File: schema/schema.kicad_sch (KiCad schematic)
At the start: 13 parts, among them Q1 2N7000, SW1 SW_Push, U1 PIC32MX170F256B, U2 NRF24L01_Breakout

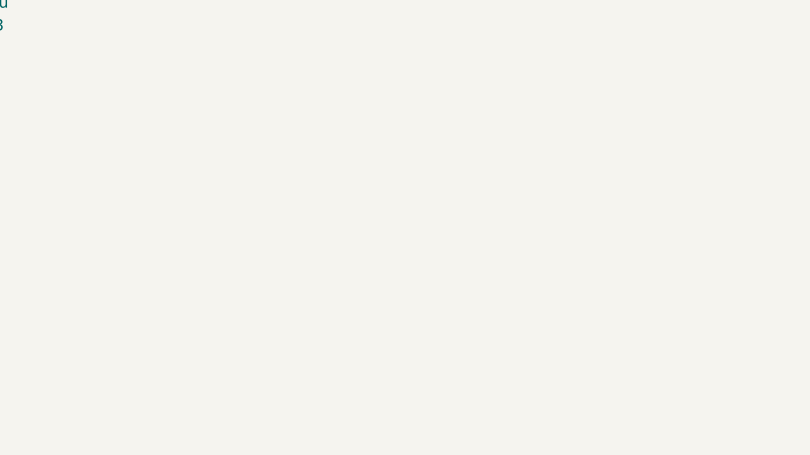
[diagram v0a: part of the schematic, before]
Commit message: Update schematic. Remote motor control working
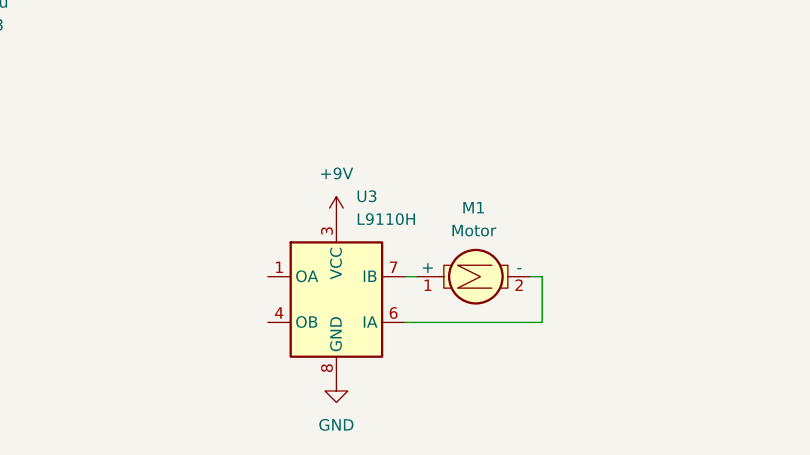
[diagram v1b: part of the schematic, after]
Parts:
- added M1: Motor, symbol ME218_BaseLib:Motor
- added U3: L9110H, Package_SO:SOIC-8_3.9x4.9mm_P1.27mm, symbol Driver_FET:HIP2100_SOIC
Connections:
- net GND: now also U3.5 (GND), U3.8 (GND)
- new net: M1.2 (-), U3.6 (IA)
- new net: M1.1 (+), U3.7 (IB)
- new net +9V: U3.2 (VCC), U3.3 (VCC)

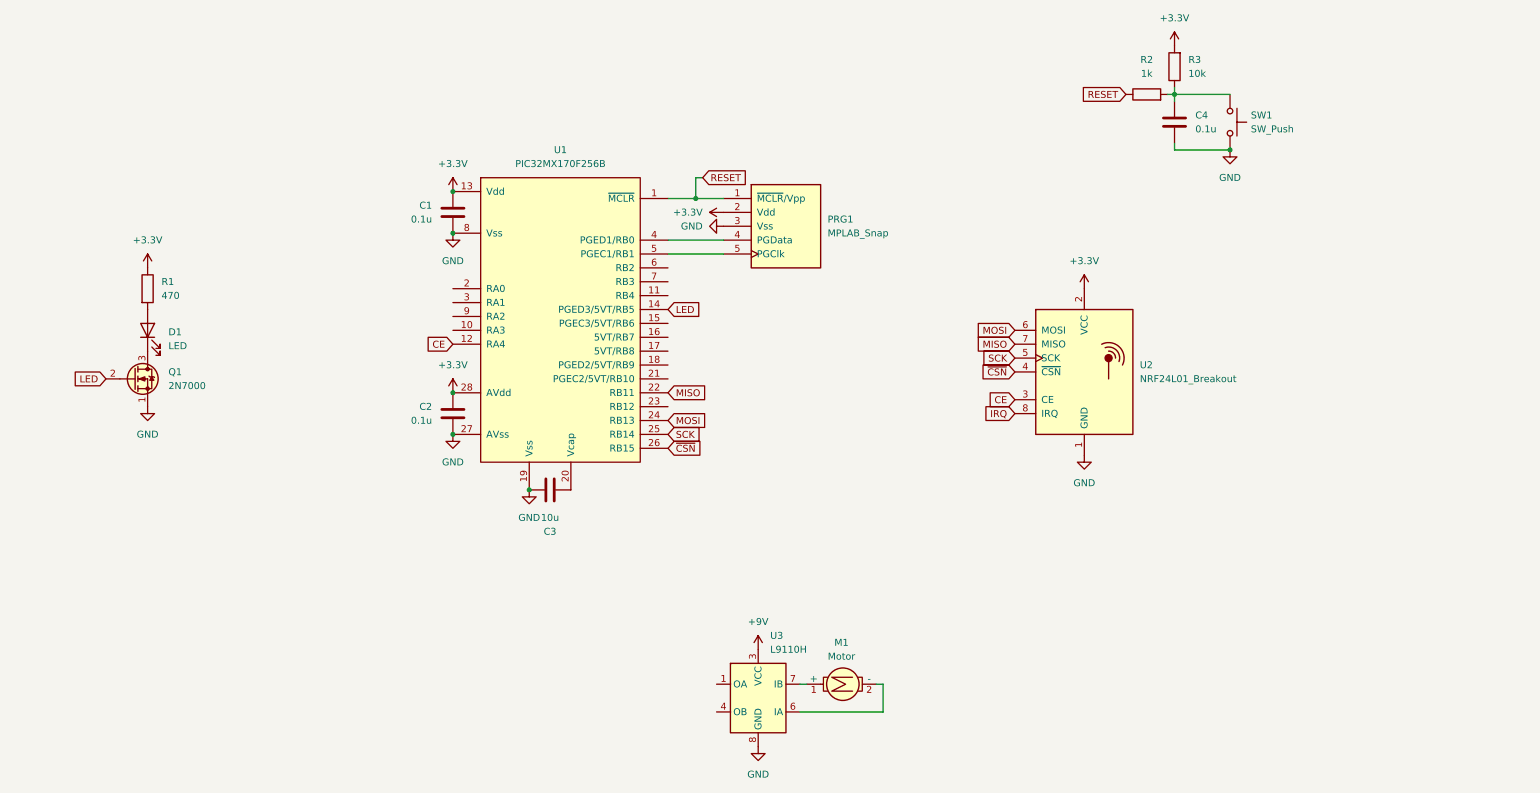
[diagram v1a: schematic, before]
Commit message: Update schematic to use PIC16 from PIC32
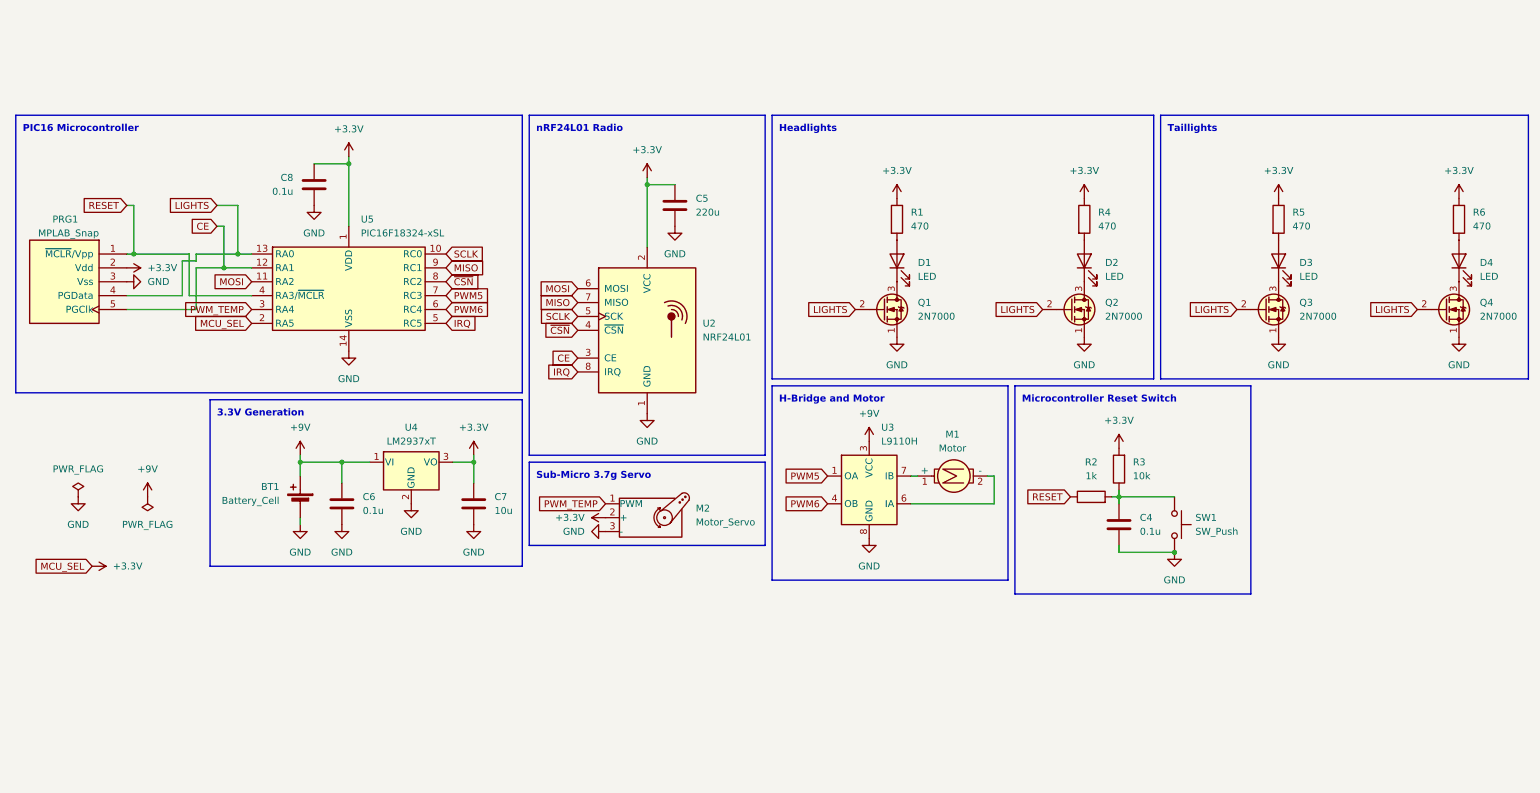
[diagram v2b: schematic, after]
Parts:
- removed C1, C2: 0.1u, symbol Device:C
- removed C3: 10u, symbol Device:C
- removed U1: PIC32MX170F256B, symbol ME218_BaseLib:PIC32MX170F256B
- added BT1: Battery_Cell, RC_Car_footprints:BAT_BH9VPC, symbol Device:Battery_Cell
- added C5: 220u, Capacitor_THT:C_Rect_L4.0mm_W2.5mm_P2.50mm, symbol Device:C
- added C6, C8: 0.1u, Capacitor_THT:C_Rect_L4.0mm_W2.5mm_P2.50mm, symbol Device:C
- added C7: 10u, Capacitor_THT:C_Rect_L4.0mm_W2.5mm_P2.50mm, symbol Device:C
- added D2, D3, D4: LED, LED_THT:LED_D5.0mm, symbol Device:LED
- added M2: Motor_Servo, Connector_PinSocket_2.54mm:PinSocket_1x03_P2.54mm_Vertical, symbol Motor:Motor_Servo
- added Q2, Q3, Q4: 2N7000, Package_TO_SOT_THT:TO-92_Inline_Wide, symbol ME218_BaseLib:2N7000
- added R4, R5, R6: 470, Resistor_THT:R_Axial_DIN0204_L3.6mm_D1.6mm_P7.62mm_Horizontal, symbol Device:R
- added U4: LM2937xT, Package_TO_SOT_THT:TO-220-3_Vertical, symbol Regulator_Linear:LM2937xT
- added U5: PIC16F18324-xSL, Package_DIP:CERDIP-14_W7.62mm_SideBrazed, symbol MCU_Microchip_PIC16:PIC16F18324-xSL
- C4: footprint (none) -> Capacitor_THT:C_Rect_L4.0mm_W2.5mm_P2.50mm
- D1: footprint (none) -> LED_THT:LED_D5.0mm
- M1: footprint (none) -> Connector_PinSocket_2.54mm:PinSocket_1x02_P2.54mm_Vertical
- PRG1: footprint (none) -> Connector_PinSocket_2.54mm:PinSocket_1x05_P2.54mm_Vertical
- Q1: footprint Package_TO_SOT_THT:TO-92_Inline -> Package_TO_SOT_THT:TO-92_Inline_Wide
- R1, R2, R3: footprint (none) -> Resistor_THT:R_Axial_DIN0204_L3.6mm_D1.6mm_P7.62mm_Horizontal
- SW1: footprint (none) -> RC_Car_footprints:SW_TS02-66-60-BK-160-LCR-D
- U2: value NRF24L01_Breakout -> NRF24L01
- U3: footprint Package_SO:SOIC-8_3.9x4.9mm_P1.27mm -> Package_DIP:DIP-8_W7.62mm_Socket
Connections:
- net LED is gone; now on net LIGHTS: Q1.2 (G)
- net +3.3V: now also C5.1, C7.1, C8.2, M2.2 (+), R4.1, R5.1, R6.1, U4.3 (VO), U5.1 (VDD), U5.2 (RA5)
- net +9V: now also BT1.1 (+), C6.1, U4.1 (VI)
- net CE: now also PRG1.5 (PGClk), U5.12 (RA1)
- net GND: now also SW1.3, SW1.4, BT1.2 (-), C5.2, C6.2, C7.2, C8.1, M2.3 (-), Q2.1 (S), Q3.1 (S), Q4.1 (S), U4.2 (GND), U5.14 (VSS); no longer SW1.2
- net IRQ: now also U5.5 (RC5)
- net MISO: now also U5.9 (RC1)
- net MOSI: now also U5.11 (RA2)
- net RESET: now also U5.4 (RA3/~{MCLR})
- net ~{CSN}: now also U5.8 (RC2)
- net at C4.1, R2.2, R3.1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: now also SW1.2
- net PWM5: now reaches U3.1 (OA)
- net PWM5: now also U5.7 (RC3)
- net PWM6: now reaches U3.4 (OB)
- net PWM6: now also U5.6 (RC4)
- net LIGHTS: now reaches PRG1.4 (PGData)
- net LIGHTS: now also Q2.2 (G), Q3.2 (G), Q4.2 (G), U5.13 (RA0)
- net SCK renamed SCLK
- net SCLK: now also U5.10 (RC0)
- new net: D2.2 (A), R4.2
- new net: D4.1 (K), Q4.3 (D)
- new net: D2.1 (K), Q2.3 (D)
- new net: D4.2 (A), R6.2
- new net: D3.2 (A), R5.2
- new net: D3.1 (K), Q3.3 (D)
- new net PWM_TEMP: M2.1 (PWM), U5.3 (RA4)
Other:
- note added: "3.3V Generation"
- note added: "H-Bridge and Motor"
- note added: "Headlights"
- note added: "Microcontroller Reset Switch"
- note added: "PIC16 Microcontroller"
- note added: "Sub-Micro 3.7g Servo"
- note added: "Taillights"
- note added: "nRF24L01 Radio"
- moved on the sheet: C4, D1, M1, Q1, R1, R2, R3, SW1, U2, U3

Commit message: Add switch to schema
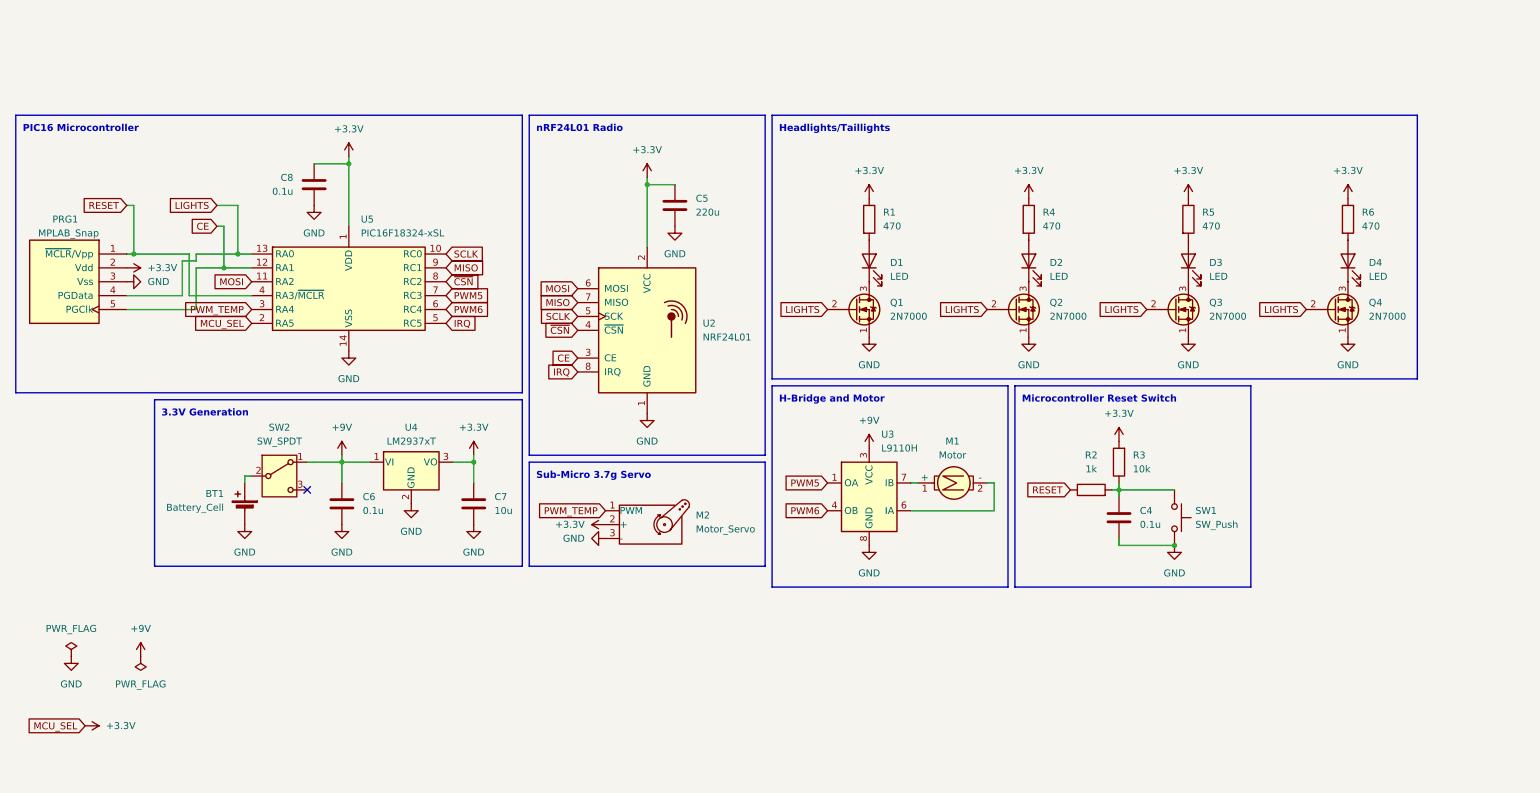
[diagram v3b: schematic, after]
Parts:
- added SW2: SW_SPDT, RC_Car_footprints:SW_EG1218, symbol Switch:SW_SPDT
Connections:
- net +9V: now also SW2.1 (A); no longer BT1.1 (+)
- new net: BT1.1 (+), SW2.2 (B)
- no-connect marks 0 -> 1
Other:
- note added: "Headlights/Taillights"
- note removed: "Headlights"
- note removed: "Taillights"
- moved on the sheet: BT1, C4, D1, D2, D3, D4, M1, M2, Q1, Q2, Q3, Q4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

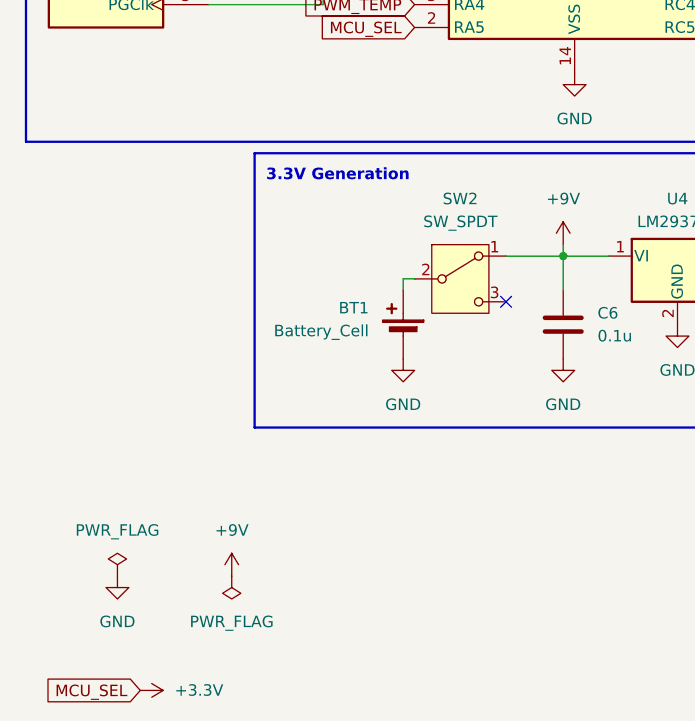
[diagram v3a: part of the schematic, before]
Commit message: Change pinout on pic16 in schematic
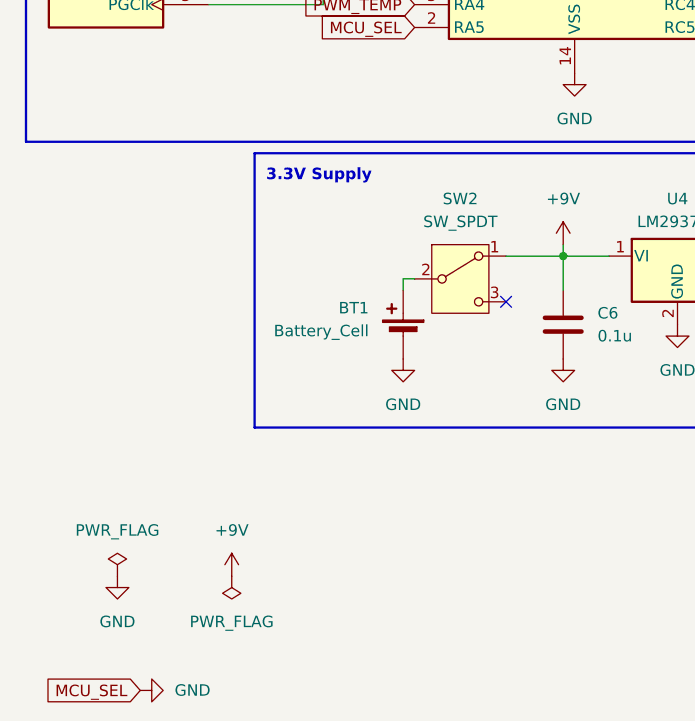
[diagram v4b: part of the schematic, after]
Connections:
- net +3.3V: no longer U5.2 (RA5)
- net GND: now also U5.2 (RA5)
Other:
- note added: "3.3V Supply"
- note removed: "3.3V Generation"
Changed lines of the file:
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@@
 		)
 	)
-	(text "3.3V Generation"
+	(text "3.3V Supply"
 		(exclude_from_sim no)
 		(at 44.45 93.98 0)
@@
 	)
 	(symbol
-		(lib_id "power:+3.3V")
-		(at 30.48 151.13 270)
-		(unit 1)
-		(exclude_from_sim no)
-		(in_bom yes)
-		(on_board yes)
-		(dnp no)
-		(fields_autoplaced yes)
-		(property "Reference" "#PWR01"
-			(at 26.67 151.13 0)
-			(effects
-				(font
-					(size 1.27 1.27)
-				)
-				(hide yes)
-			)
-		)
-		(property "Value" "+3.3V"
-			(at 34.29 151.1299 90)
-			(effects
-				(font
-					(size 1.27 1.27)
-				)
-				(justify left)
-			)
-		)
-		(property "Footprint" ""
-			(at 30.48 151.13 0)
-			(effects
-				(font
-					(size 1.27 1.27)
-				)
-				(hide yes)
-			)
-		)
-		(property "Datasheet" ""
-			(at 30.48 151.13 0)
-			(effects
-				(font
-					(size 1.27 1.27)
-				)
-				(hide yes)
-			)
-		)
-		(property "Description" "Power symbol creates a global label with name \"+3.3V\""
-			(at 30.48 151.13 0)
-			(effects
-				(font
-					(size 1.27 1.27)
-				)
-				(hide yes)
-			)
-		)
-		(pin "1"
-		)
-		(instances
-			(project "schema"
-				(path "/234e0340-f69a-4400-80a5-91e7204dda97"
-					(reference "#PWR01")
-					(unit 1)
-				)
-			)
-		)
-	)
-	(symbol
 		(lib_id "power:GND")
 		(at 38.1 69.85 90)
@@
 					(unit 1)
 				)
+			)
+		)
+	)
+	(symbol
+		(lib_id "power:GND")
+		(at 30.48 151.13 90)
+		(unit 1)
+		(exclude_from_sim no)
+		(in_bom yes)
+		(on_board yes)
+		(dnp no)
+		(fields_autoplaced yes)
+		(property "Reference" "#PWR01"
+			(at 36.83 151.13 0)
+			(effects
+				(font
+					(size 1.27 1.27)
+				)
+				(hide yes)
+			)
+		)
+		(property "Value" "GND"
+			(at 34.29 151.1299 90)
+			(effects
+				(font
+					(size 1.27 1.27)
+				)
+				(justify right)
+			)
+		)
+		(property "Footprint" ""
+			(at 30.48 151.13 0)
+			(effects
+				(font
+					(size 1.27 1.27)
+				)
+				(hide yes)
+			)
+		)
+		(property "Datasheet" ""
+			(at 30.48 151.13 0)
+			(effects
+				(font
+					(size 1.27 1.27)
+				)
+				(hide yes)
+			)
+		)
+		(property "Description" "Power symbol creates a global label with name \"GND\" , ground"
+			(at 30.48 151.13 0)
+			(effects
+				(font
+					(size 1.27 1.27)
+				)
+				(hide yes)
+			)
+		)
+		(pin "1"
+		)
+		(instances
+			(project "schema"
+				(path "/234e0340-f69a-4400-80a5-91e7204dda97"
+					(reference "#PWR01")
+					(unit 1)
+				)

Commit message: Refactors schematics
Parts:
- added D5: LED, LED_THT:LED_D5.0mm, symbol Device:LED
- added R7: 470, Resistor_THT:R_Axial_DIN0204_L3.6mm_D1.6mm_P7.62mm_Horizontal, symbol Device:R
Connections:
- net +9V: now also R7.1
- net GND: now also D5.1 (K)
- net MOSI: now also U5.3 (RA4); no longer U5.11 (RA2)
- net PWM5: now also U5.8 (RC2); no longer U5.7 (RC3)
- net PWM6: now also M2.1 (PWM), U5.11 (RA2); no longer U3.4 (OB), U5.6 (RC4)
- net ~{CSN}: now also U5.7 (RC3); no longer U5.8 (RC2)
- removed net PWM_TEMP: M2.1 (PWM), U5.3 (RA4)
- new net: D5.2 (A), R7.2
- new net PWM5.1: U3.4 (OB), U5.6 (RC4)
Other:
- moved on the sheet: BT1, SW2
